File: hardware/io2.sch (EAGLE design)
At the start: 25 parts, among them IC1 PCF8574T, Q1 BC857BSMD, Q2 BSS123, Q3 BSS123

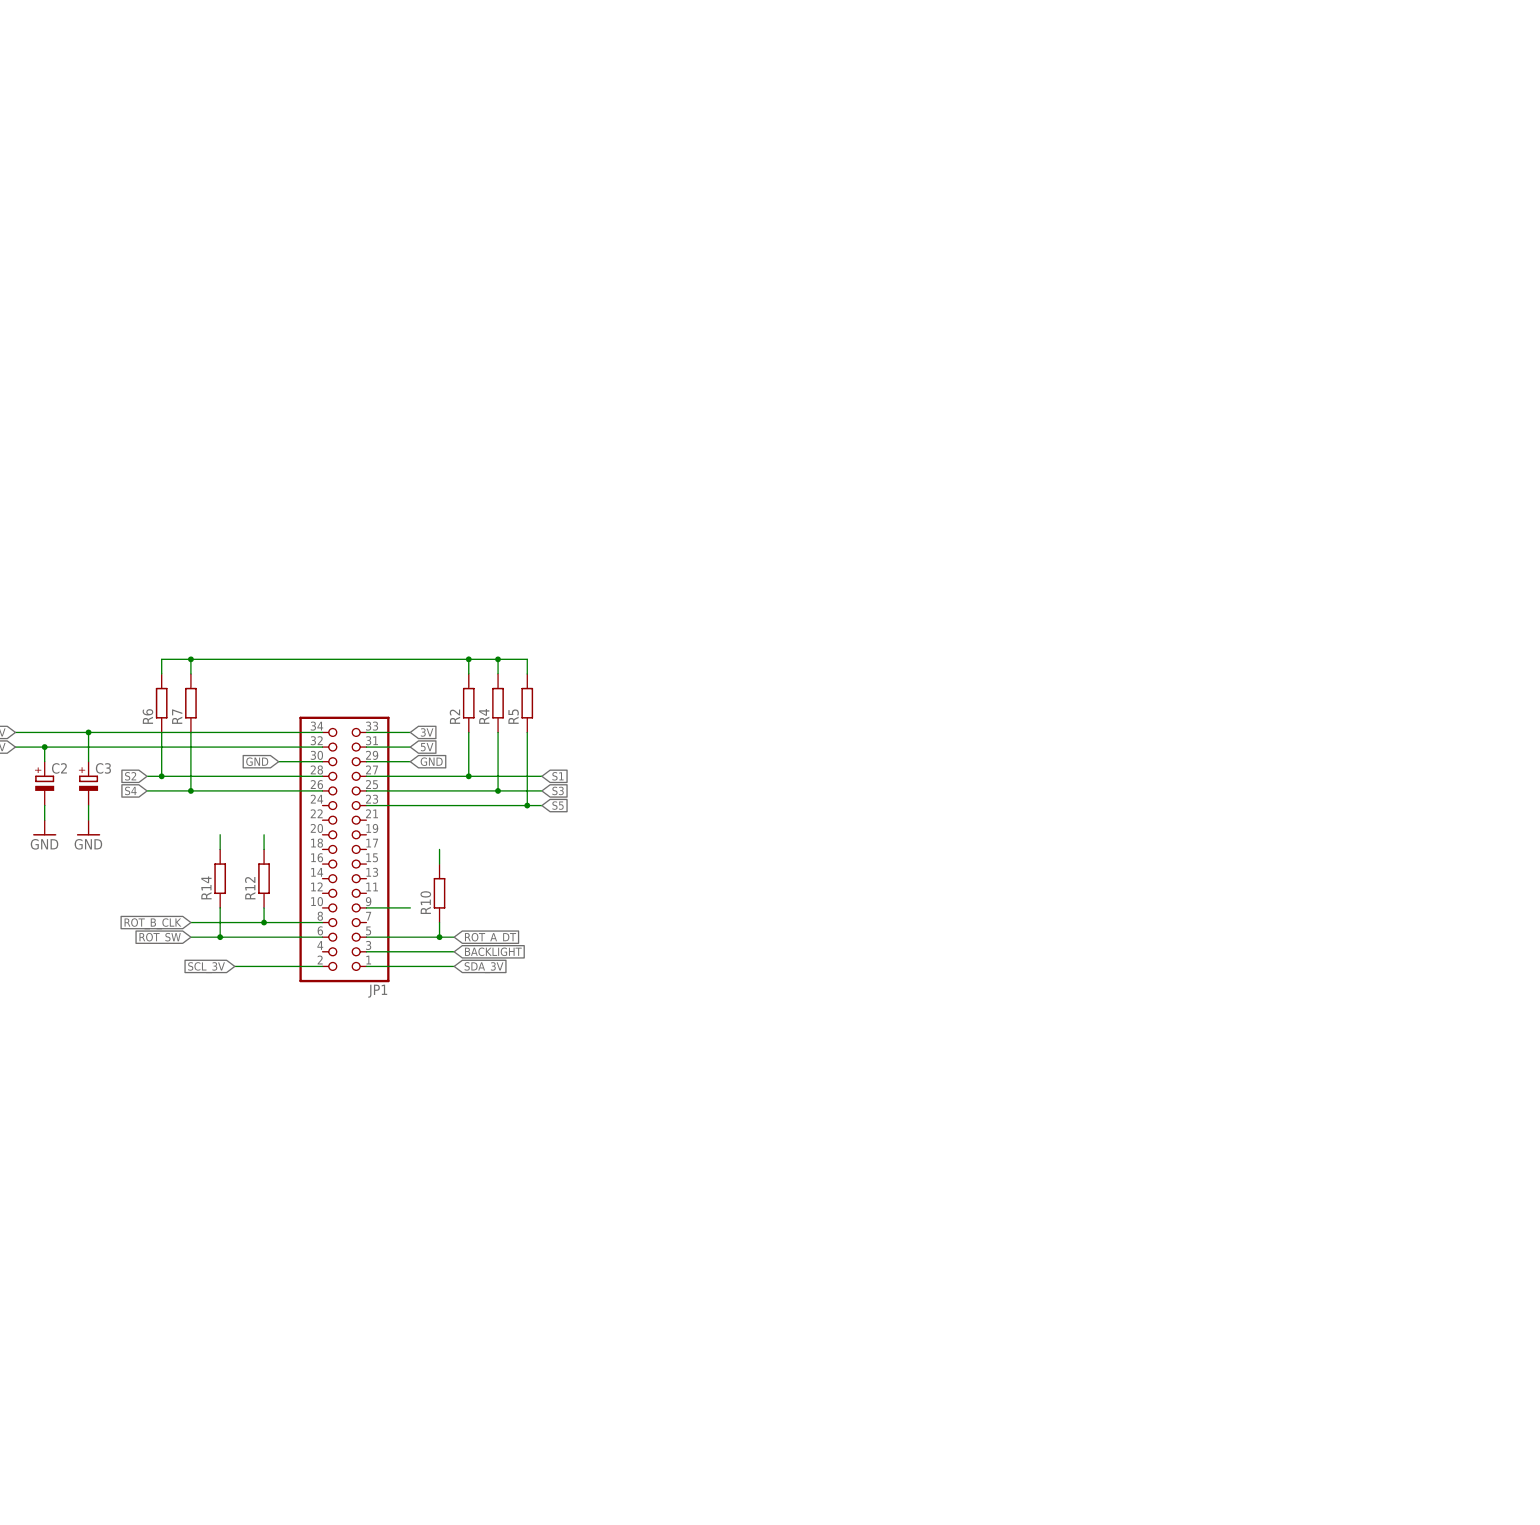
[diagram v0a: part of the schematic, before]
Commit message: Rotary encoder debounce
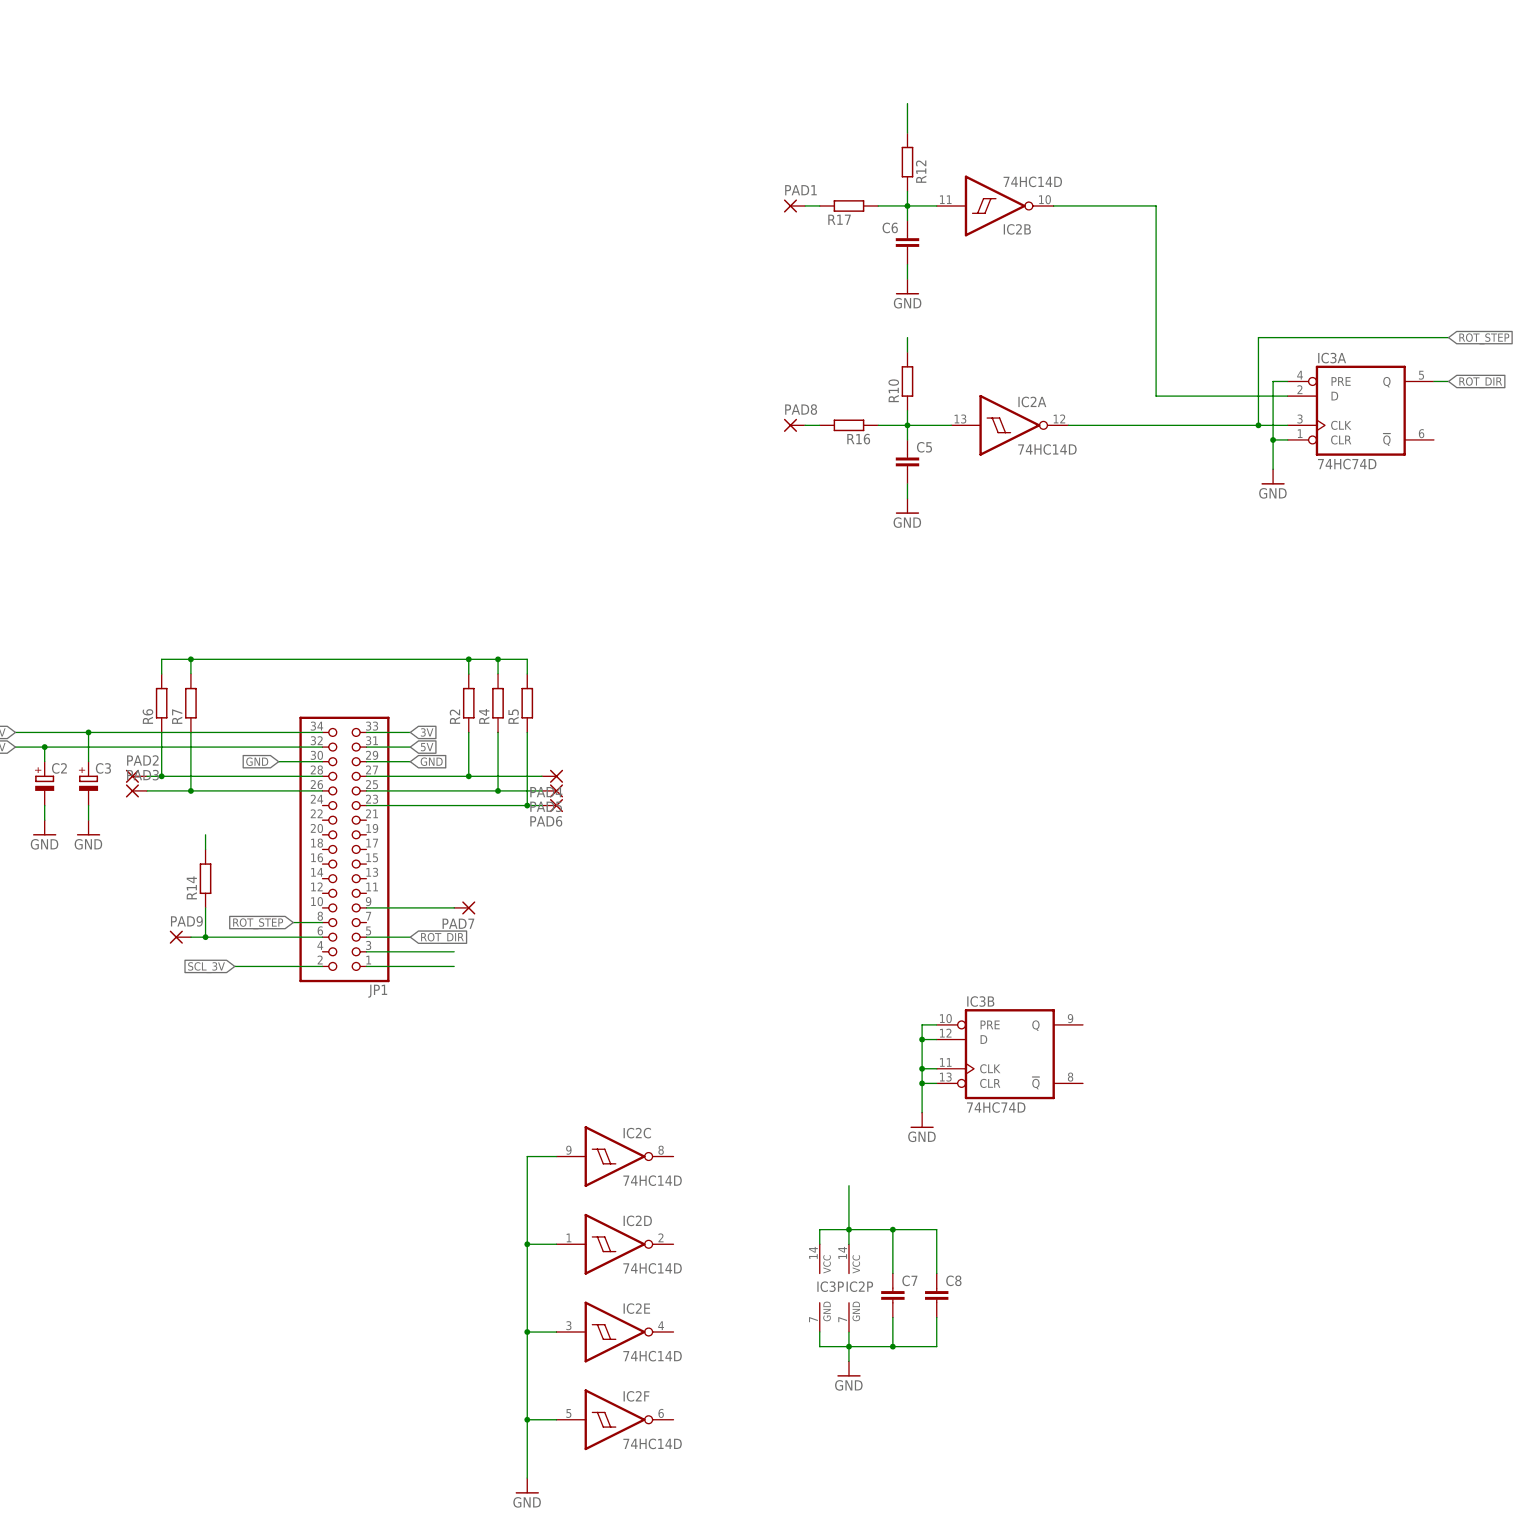
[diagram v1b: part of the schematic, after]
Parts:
- added C5, C6, C7, C8: (no value), rcl:C-EUC0603
- added IC2: 74HC14D, 74xx-eu:74HC14D
- added IC3: 74HC74D, 74xx-eu:74HC74D
- added PAD1, PAD2, PAD3, PAD4, PAD5, PAD6, PAD7, PAD8, PAD9: (no value), wirepad:SMD2
- added R16, R17: (no value), rcl:R-EU_R0603
- R14: device rcl:R-EU_0204/7 -> rcl:R-EU_0204/5
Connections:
- new net N$5: PAD8.P, R16.2
- new net N$7: PAD1.P, R17.1
- new net ROT_B_: IC2B.O, IC3A.D
- new net ROT_DIR: IC3A.Q, JP1.5
- new net ROT_STEP: IC2A.O, IC3A.CLK, JP1.8
- net 3V: now also C7.1, C8.1, IC2P.VCC, IC3P.VCC
- net GND: now also C5.2, C6.2, C7.2, C8.2, IC2C.I, IC2D.I, IC2E.I, IC2F.I, IC2P.GND, IC3A.CLR, IC3A.PRE, IC3B.CLK, IC3B.CLR, IC3B.D, IC3B.PRE, IC3P.GND
- net IR_DATA: now also PAD7.P
- net ROT_A_DT: now also C5.1, IC2A.I, R16.1; no longer JP1.5
- net ROT_B_CLK: now also C6.1, IC2B.I, R17.2; no longer JP1.8
- net ROT_SW: now also PAD9.P
- net S1: now also PAD4.P
- net S2: now also PAD2.P
- net S3: now also PAD5.P
- net S4: now also PAD3.P
- net S5: now also PAD6.P
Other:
- moved on the sheet: R10, R12, R14

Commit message: Backlight fixed
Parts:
- R13: device rcl:R-EU_0204/7 -> rcl:R-EU_0207/12
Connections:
- net BACKLIGHT: now also IC1.P0; no longer JP1.3
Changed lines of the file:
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@@
 <part name="R11" library="pot" deviceset="TRIM_EU-" device="B25U"/>
 <part name="GND5" library="supply1" deviceset="GND" device=""/>
-<part name="R13" library="rcl" deviceset="R-EU_" device="0204/7"/>
+<part name="R13" library="rcl" deviceset="R-EU_" device="0207/12"/>
 <part name="Q1" library="transistor-pnp" deviceset="BC857*" device="SMD" technology="B"/>
 <part name="R9" library="rcl" deviceset="R-EU_" device="R0603" value="4k7"/>
@@
 <wire x1="185.42" y1="162.56" x2="200.66" y2="162.56" width="0.1524" layer="91"/>
 <pinref part="JP1" gate="A" pin="1"/>
+<label x="200.66" y="162.56" size="1.4224" layer="95" xref="yes"/>
 </segment>
 </net>
@@
 <net name="BACKLIGHT" class="0">
 <segment>
-<pinref part="JP1" gate="A" pin="3"/>
-<wire x1="185.42" y1="165.1" x2="200.66" y2="165.1" width="0.1524" layer="91"/>
-</segment>
-<segment>
 <pinref part="R13" gate="G$1" pin="2"/>
 <wire x1="0" y1="111.76" x2="-2.54" y2="111.76" width="0.1524" layer="91"/>
 <label x="-2.54" y="111.76" size="1.4224" layer="95" rot="R180" xref="yes"/>
 </segment>
-</net>
+<segment>
+<pinref part="IC1" gate="G$1" pin="P0"/>
+<wire x1="-33.02" y1="129.54" x2="-25.4" y2="129.54" width="0.1524" layer="91"/>
+<label x="-25.4" y="129.54" size="1.4224" layer="95" xref="yes"/>
+</segment>
+</net>

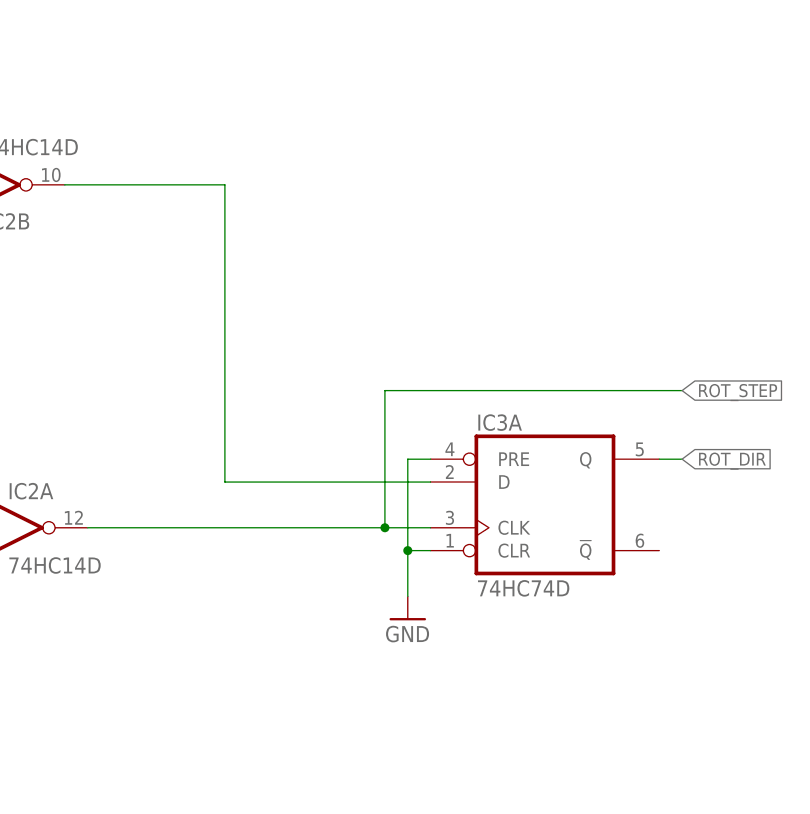
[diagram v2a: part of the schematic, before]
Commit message: rotary encoder fixed
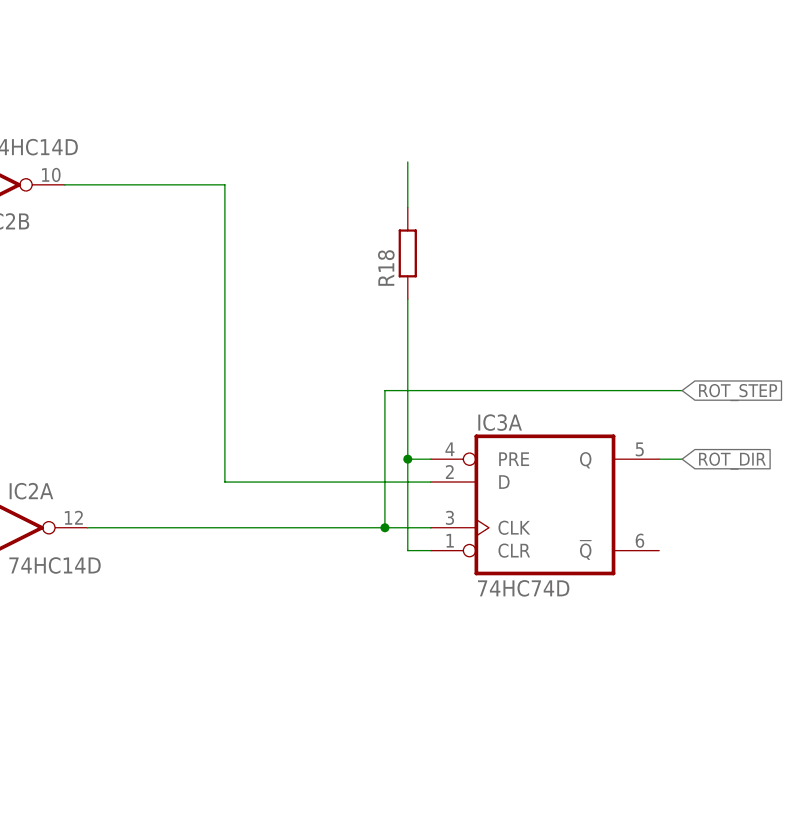
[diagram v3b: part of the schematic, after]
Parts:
- added R18: (no value), rcl:R-EU_0204/7
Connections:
- new net N$2: IC3A.CLR, IC3A.PRE, R18.1
- net 3V: now also R18.2
- net GND: no longer IC3A.CLR, IC3A.PRE
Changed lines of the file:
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@@
 <part name="C7" library="rcl" deviceset="C-EU" device="C0603"/>
 <part name="IC3" library="74xx-eu" deviceset="74*74" device="D" technology="HC"/>
-<part name="GND9" library="supply1" deviceset="GND" device=""/>
 <part name="GND10" library="supply1" deviceset="GND" device=""/>
 <part name="C8" library="rcl" deviceset="C-EU" device="C0603"/>
 <part name="PAD1" library="wirepad" deviceset="SMD2" device=""/>
 <part name="PAD8" library="wirepad" deviceset="SMD2" device=""/>
+<part name="R18" library="rcl" deviceset="R-EU_" device="0204/7"/>
 </parts>
 <sheets>
@@
 <instance part="C7" gate="G$1" x="276.86" y="106.68"/>
 <instance part="IC3" gate="A" x="358.14" y="259.08"/>
-<instance part="GND9" gate="1" x="342.9" y="246.38"/>
 <instance part="IC3" gate="B" x="297.18" y="147.32"/>
 <instance part="GND10" gate="1" x="281.94" y="134.62"/>
@@
 <instance part="PAD1" gate="1" x="259.08" y="294.64"/>
 <instance part="PAD8" gate="1" x="259.08" y="256.54"/>
+<instance part="R18" gate="G$1" x="342.9" y="287.02" rot="R90"/>
 </instances>
 <busses>
@@
 </segment>
 <segment>
-<pinref part="IC3" gate="A" pin="PRE"/>
-<pinref part="GND9" gate="1" pin="GND"/>
-<wire x1="345.44" y1="264.16" x2="342.9" y2="264.16" width="0.1524" layer="91"/>
-<wire x1="342.9" y1="264.16" x2="342.9" y2="254" width="0.1524" layer="91"/>
-<pinref part="IC3" gate="A" pin="CLR"/>
-<wire x1="342.9" y1="254" x2="342.9" y2="248.92" width="0.1524" layer="91"/>
-<wire x1="345.44" y1="254" x2="342.9" y2="254" width="0.1524" layer="91"/>
-<junction x="342.9" y="254"/>
-</segment>
-<segment>
 <pinref part="IC3" gate="B" pin="PRE"/>
 <pinref part="GND10" gate="1" pin="GND"/>
@@
 <junction x="276.86" y="116.84"/>
 </segment>
+<segment>
+<pinref part="R18" gate="G$1" pin="2"/>
+<wire x1="342.9" y1="292.1" x2="342.9" y2="297.18" width="0.1524" layer="91"/>
+</segment>
 </net>
 <net name="BACKLIGHT" class="0">
@@
 </segment>
 </net>
+<net name="N$2" class="0">
+<segment>
+<pinref part="IC3" gate="A" pin="PRE"/>
+<wire x1="345.44" y1="264.16" x2="342.9" y2="264.16" width="0.1524" layer="91"/>
+<wire x1="342.9" y1="264.16" x2="342.9" y2="254" width="0.1524" layer="91"/>
+<pinref part="IC3" gate="A" pin="CLR"/>
+<wire x1="345.44" y1="254" x2="342.9" y2="254" width="0.1524" layer="91"/>
+<wire x1="342.9" y1="264.16" x2="342.9" y2="281.94" width="0.1524" layer="91"/>
+<junction x="342.9" y="264.16"/>
+<pinref part="R18" gate="G$1" pin="1"/>
+</segment>
+</net>
